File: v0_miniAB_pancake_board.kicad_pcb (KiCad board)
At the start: 2 copper layers, 51.5 x 37.4 mm, 15 parts, among them J1 Conn_01x04_Female, J10 Conn_01x03_Female, J11 Conn_01x03_Female, J2 Conn_01x02_Female, J3 Conn_01x04_Female, J4 Conn_01x02_Female, J5 Conn_01x02_Female, J6 Conn_01x02_Female, J7 Conn_01x03_Female, J8 Conn_01x03_Female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

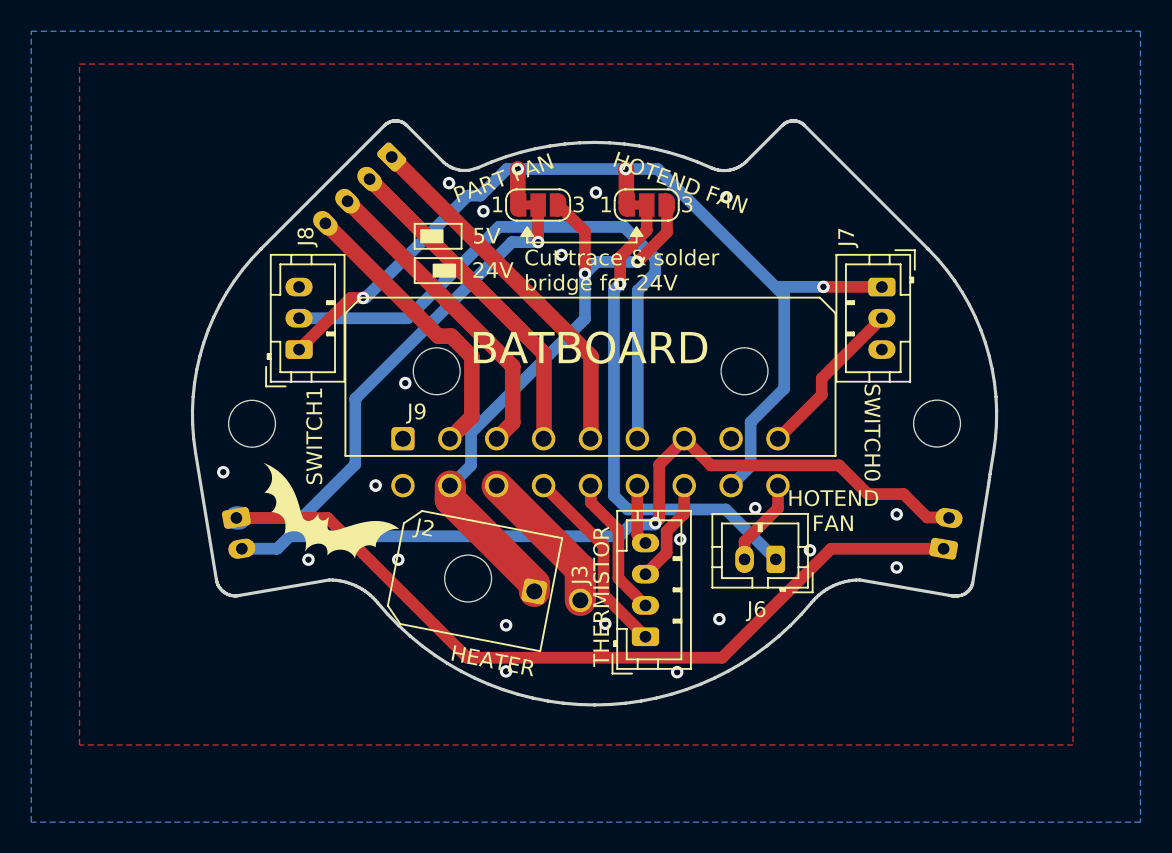
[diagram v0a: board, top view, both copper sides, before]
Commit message: Moved some things, added CT, checked clearance
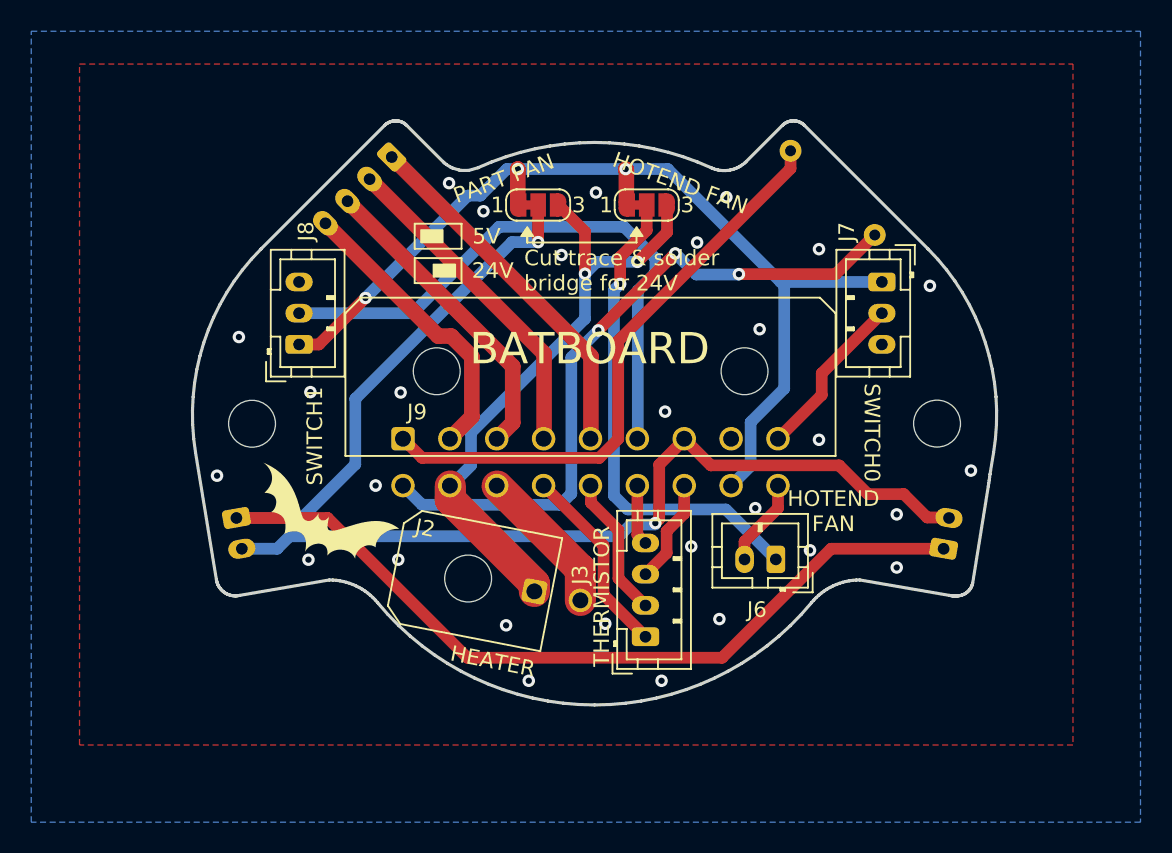
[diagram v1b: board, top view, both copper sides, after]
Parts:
- added TH1: Thermistor_NTC, Resistor_THT:R_Axial_DIN0204_L3.6mm_D1.6mm_P7.62mm_Horizontal, B.Cu at (112.7, 82.5)
- moved J7 0.33 mm to (118.5, 90.9)
- moved J8 0.33 mm to (81.2, 94.9)
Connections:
- J9 pad 1: unconnected-(J9-Pad1) -> /ctherm0
- J9 pad 10: unconnected-(J9-Pad10) -> /ctherm1
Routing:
- net /ctherm1: track 0.00 -> 44.2 mm, vias 0 -> 3
- net /ctherm0: track 0.00 -> 37.8 mm
- net +5V: track 64.0 -> 64.2 mm, vias 4 -> 3
- net GND: vias 20 -> 29
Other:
- board text added: "CTH0 A+ A- B+ B- SW1 FAN0 GND SW0"
- board text added: "CTH1 24V HEAT_GND TH0 TH1 TH3 TH2 5V FAN1"
- board text removed: "24V HEAT_GND TH0 TH1 SW0 FAN1 5V"
- board text removed: "A+ A- B+ B- SW1 FAN0 GND"
